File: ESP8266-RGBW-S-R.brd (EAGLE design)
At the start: 95.5 x 55.1 mm, 57 parts, among them IC1 ATTINY85, IC2 ESP8266-ESP12, IC6 LM1117-3.3, K1 SONGLE-RELAY-SPDT, K2 OMRON-G3MB-OPTO-RELAY, Q1 BC317, Q2 BC317, Q3 SO340020, Q4 SO340020, Q5 SO340020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

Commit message: added White channel for PWM output
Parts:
- removed JP4: (no value), Aidans:HDR4X0.1
- added J1: DCJ0202, con-jack:DCJ0202
- added Q6: SO340020, transistor-fet:SOT23
- added R20: 1K, resistor:R0805
- added X1: JST-XH-05-PIN-LONG-PAD, Rembrandt Electronics - JST XH Connectors v1-0:JST-XH-05-PACKAGE-LONG-PAD
- moved R19 8.98 mm to (52.5, 7.90)
- moved Q3 7.11 mm to (53.6, 14.5)
- moved Q4 7.11 mm to (58.3, 14.4)
- moved Q5 6.86 mm to (62.7, 14.4)
- moved R18 4.33 mm to (46.7, 9.75)
- moved R17 2.55 mm to (55.6, 8.92)
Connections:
- removed net N$152: IC2.TXD, JP10.5, WIFI2.1
- new net GPIO3: IC2.TXD, JP10.5, R20.2, WIFI2.1
- new net N$117: Q3.3, X1.5
- new net N$118: Q6.1, R20.1
- net GND: now also J1.3, Q6.2
- net N$12: now also Q6.3, X1.2; no longer JP4.4, Q3.3
- net N$14: now also Q5.3, X1.3; no longer JP4.3, Q4.3
- net N$79: now also Q4.3, X1.4; no longer JP4.2, Q5.3
- net N$80: now also X1.1; no longer JP4.1
- net VCC: now also J1.1
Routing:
- net GPIO3: track 0.00 -> 107.8 mm, vias 0 -> 1
- net N$152: track 33.8 -> 0.00 mm
- net N$117: track 0.00 -> 27.8 mm
- net GPIO4: track 87.4 -> 73.7 mm, vias 5 -> 4
- net N$3: track 16.6 -> 30.1 mm
- net N$81: track 13.3 -> 0.00 mm
- net GND: track 118.1 -> 107.0 mm, vias 6 -> 9
- net GPIO15: track 99.7 -> 94.6 mm
- net N$118: track 0.00 -> 4.47 mm
- net GPIO5: track 62.3 -> 58.1 mm
- net N$12: track 21.5 -> 17.6 mm
- net N$113: track 4.03 -> 7.29 mm
- net N$112: track 16.0 -> 18.5 mm
- net N$79: track 19.2 -> 21.4 mm
- net N$80: track 3.55 -> 4.67 mm
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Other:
- board text added: "W"

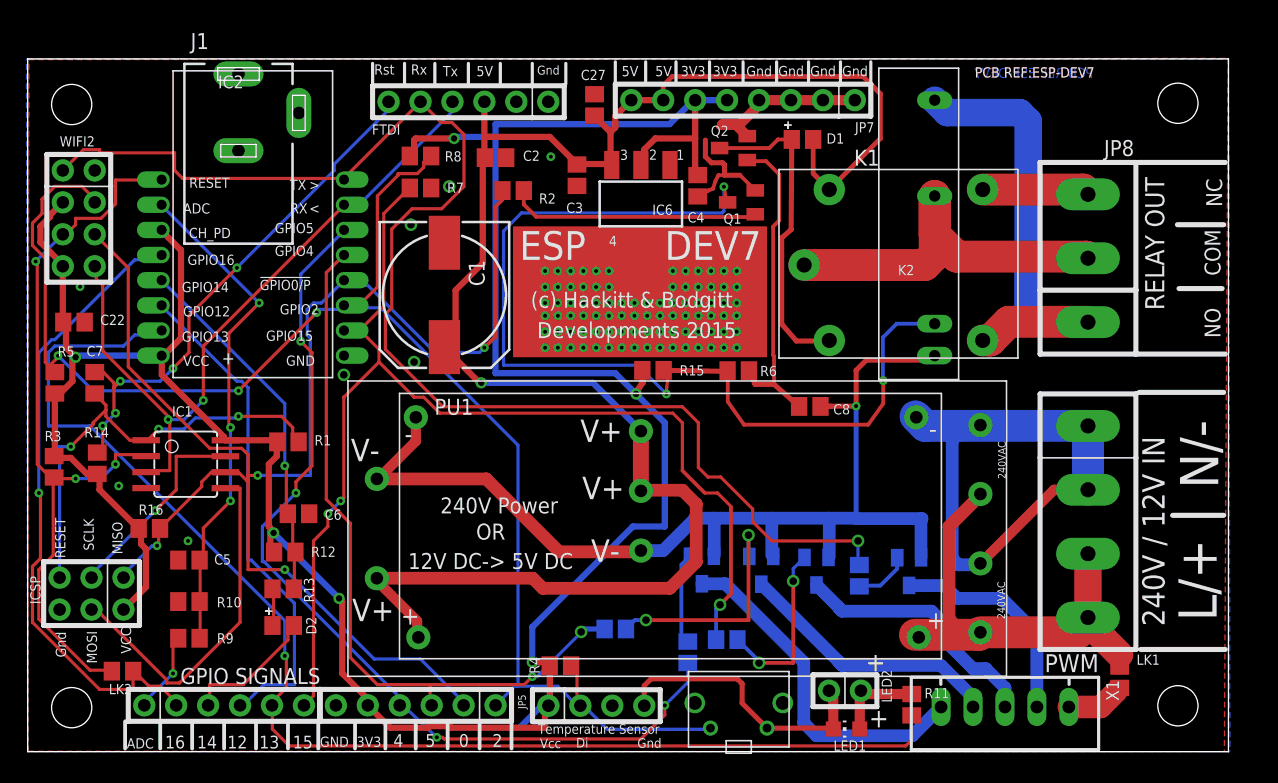
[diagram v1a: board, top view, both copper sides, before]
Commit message: alternative power subbly (DC-DC, AC-DC), alternative power jack as input
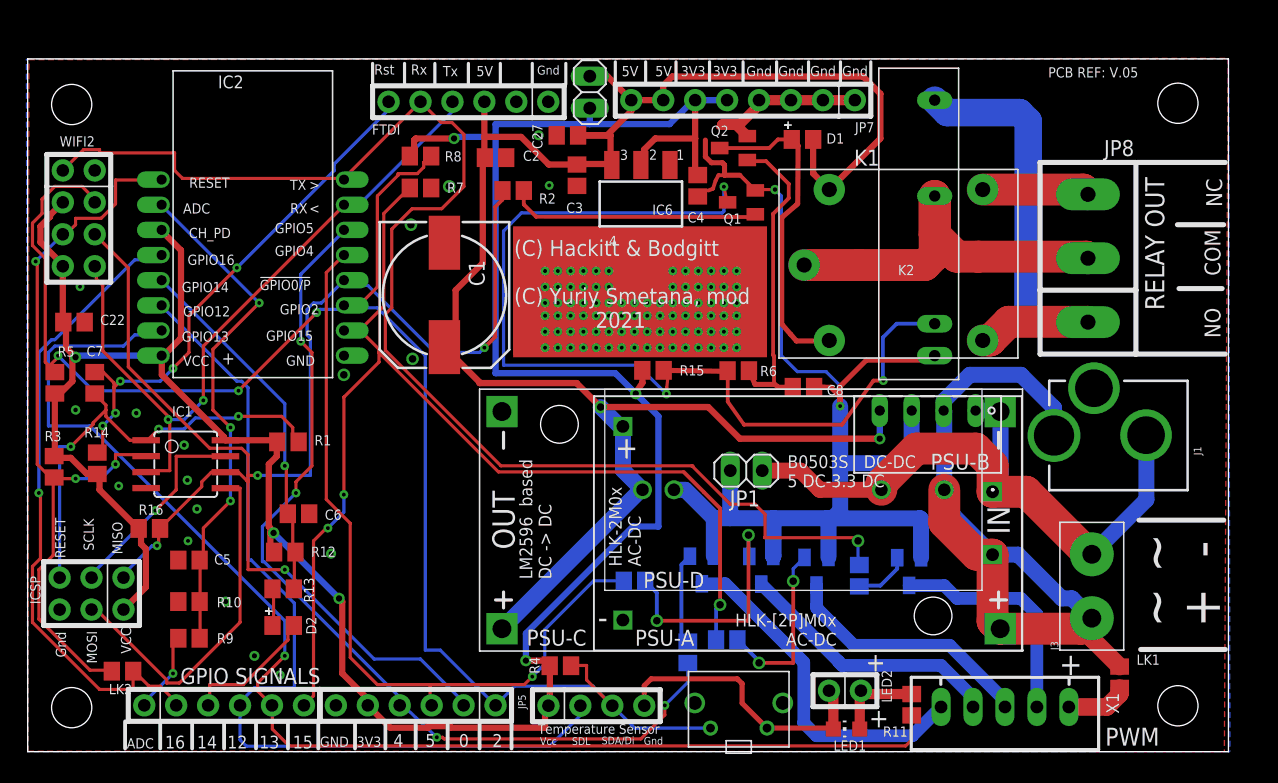
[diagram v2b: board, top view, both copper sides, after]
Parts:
- removed PU1: MAINS_PSU_CHEAP_CHINESE, Aidans:MAINS_PSU_CHEAP_CHINESE
- added J3: WJ300-5.0, SparkFun-Connectors-2pin:1X02_XTRA_BIG
- added JP4: V+V, pinhead:1X02
- added PSU-A: HLK-PM013W, 5:HLK-PM01
- added PSU-B: B0503S, dc-dc-converter:NME
- added PSU-C: DC-DC-STEP-DOWN-LM2596, diy-modules:DC-DC-STEP-DOWN-LM2596
- added PSU-D: HLK-2M03, HLK-2M03:HLK2M03
- J1: value DCJ0202 -> POWER_JACKPTH_LOCK; device con-jack:DCJ0202 -> SparkFun-Connectors:POWER_JACK_PTH_LOCK
- JP1: value 240V In -> GND+GND; device Aidans:4X0.2 -> pinhead:1X02
- moved J1 82.8 mm to (95.5, 25.1), turned to 90 degrees
- moved JP1 27.4 mm to (57.1, 22.4)
- moved R18 4.10 mm to (48.3, 13.6)
- moved C27 3.24 mm to (42.9, 49.0), turned to 180 degrees
- moved C8 1.61 mm to (61.7, 29.0)
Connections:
- removed net N$3: JP1.1, JP1.2, PU1.240V-A
- removed net N$5: JP1.3, JP1.4, LK1.1, PU1.240V-B
- new net +VCC: C1.+, C2.1, C27.1, C3.1, D1.C, IC6.3, JP10.3, JP4.1, JP7.7, JP7.8, K1.C1, PSU-A.P$4
- new net V+: J1.PWR, J3.1, LK1.1, PSU-A.P$1, PSU-B.2, PSU-C.IN+, PSU-D.1
- new net V-: J1.GND, J3.2, PSU-A.P$2, PSU-B.1, PSU-C.IN-, PSU-D.2
- net +3V3: now also JP4.2
- net GND: now also JP1.1, JP1.2, PSU-A.P$3, PSU-B.3, PSU-C.OUT-, PSU-D.3; no longer J1.3, PU1.V-
- net GPIO2: now also JP5.3; no longer JP5.2
- net N$11: now also JP5.2
- net VCC: now also PSU-B.4, PSU-C.OUT+, PSU-D.4; no longer C1.+, C2.1, C27.1, C3.1, D1.C, IC6.3, J1.1, JP10.3, JP7.7, JP7.8, K1.C1, PU1.V+
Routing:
- net +VCC: track 0.00 -> 125.1 mm, vias 0 -> 2
- net VCC: track 93.8 -> 21.5 mm, vias 1 -> 0
- net V-: track 0.00 -> 63.1 mm
- net V+: track 0.00 -> 62.8 mm
- net GND: track 107.0 -> 143.5 mm, vias 9 -> 20
- net N$11: track 39.9 -> 72.0 mm
- net N$3: track 30.1 -> 0.00 mm
- net N$5: track 18.9 -> 0.00 mm
- net N$114: track 5.11 -> 0.00 mm
- net GPIO5: track 58.1 -> 62.8 mm, vias 2 -> 1
- net GPIO2: track 125.7 -> 129.5 mm
- net GPIO15: track 94.6 -> 91.4 mm
- net +3V3: track 224.0 -> 222.2 mm
- net GPIO3: track 107.8 -> 106.4 mm
- net N$2: track 39.9 -> 40.9 mm
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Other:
- board text added: "(C) Hackitt & Bodgitt (C) Yuriy Smetana, mod 2021"
- board text added: "5V+3V3"
- board text added: "B0503S 5 DC-3.3 DC"
- board text added: "HLK-2M0x AC-DC"
- board text added: "HLK-[2P]M0x AC-DC"
- board text added: "LM2596 based DC -> DC"
- board text added: "PCB REF: V.05"
- board text added: "SDA/Di"
- board text added: "SDL"
- board text added: "~ ~ + -"
- board text removed: "(c) Hackitt & Bodgitt"
- board text removed: "12V DC-> 5V DC"
- board text removed: "240V / 12V IN"
- board text removed: "240V Power"
- board text removed: "DEV7"
- board text removed: "Developments 2015"
- board text removed: "Di"
- board text removed: "ESP"
- board text removed: "L/+"
- board text removed: "N/-"
- board text removed: "OR"
- board text removed: "PCB REF:ESP-DEV7"

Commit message: v 0.6
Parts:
- added R21: 4K7, resistor:R0805
- moved R5 50.7 mm to (47.4, 6.58), turned to 0 degrees
- moved R4 46.1 mm to (2.16, 29.3), turned to 270 degrees
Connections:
- net +3V3: now also R21.2, R4.2, R5.1; no longer R4.1, R5.2
- net GPIO2: now also R4.1, R5.2; no longer R4.2, R5.1
- net N$11: now also R21.1
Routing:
- net +3V3: track 222.2 -> 230.3 mm
- net N$11: track 72.0 -> 75.0 mm
- net GPIO2: track 129.5 -> 126.6 mm
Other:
- board text added: "+12"
- board text added: "B0503S 5DC-3.3DC"
- board text added: "PCB REF: V.06"
- board text added: "SDA Di"
- board text removed: "B0503S 5 DC-3.3 DC"
- board text removed: "PCB REF: V.05"
- board text removed: "SDA/Di"

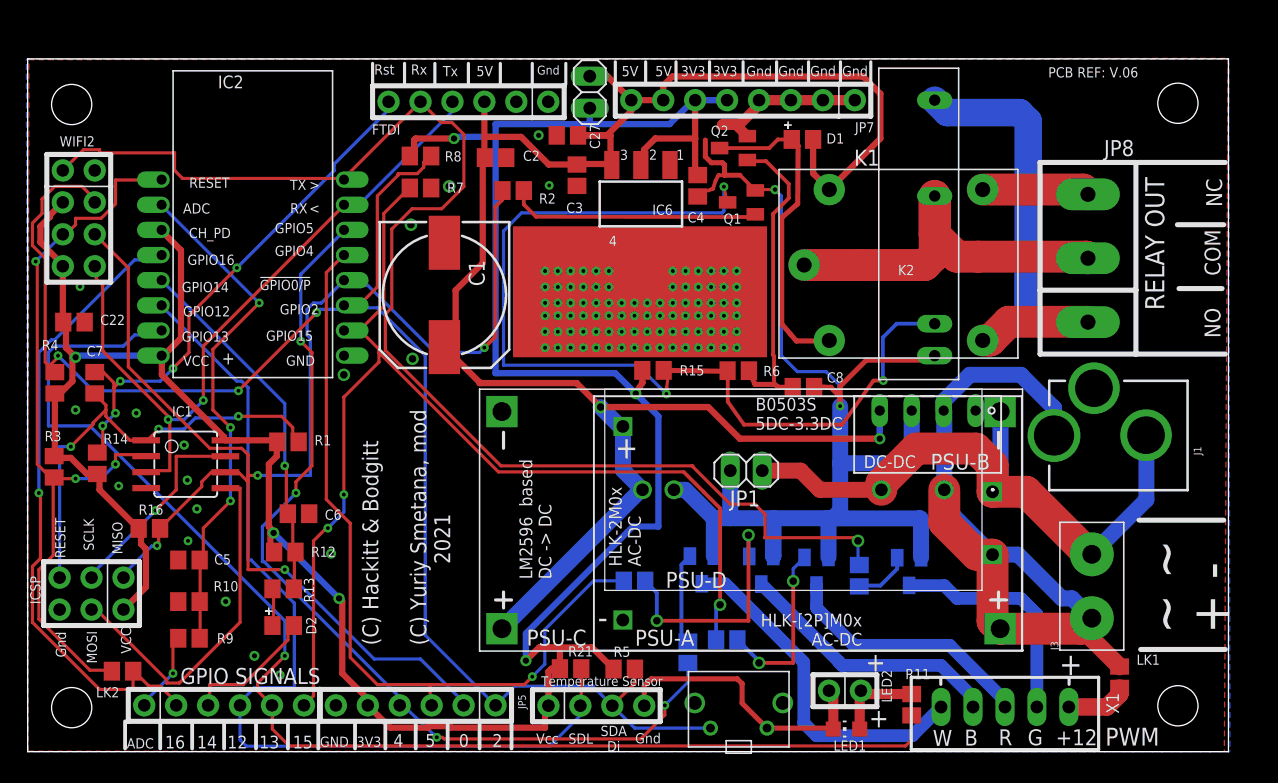
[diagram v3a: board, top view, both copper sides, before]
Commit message: pull down resistors for the PWM control, some silkprint correction
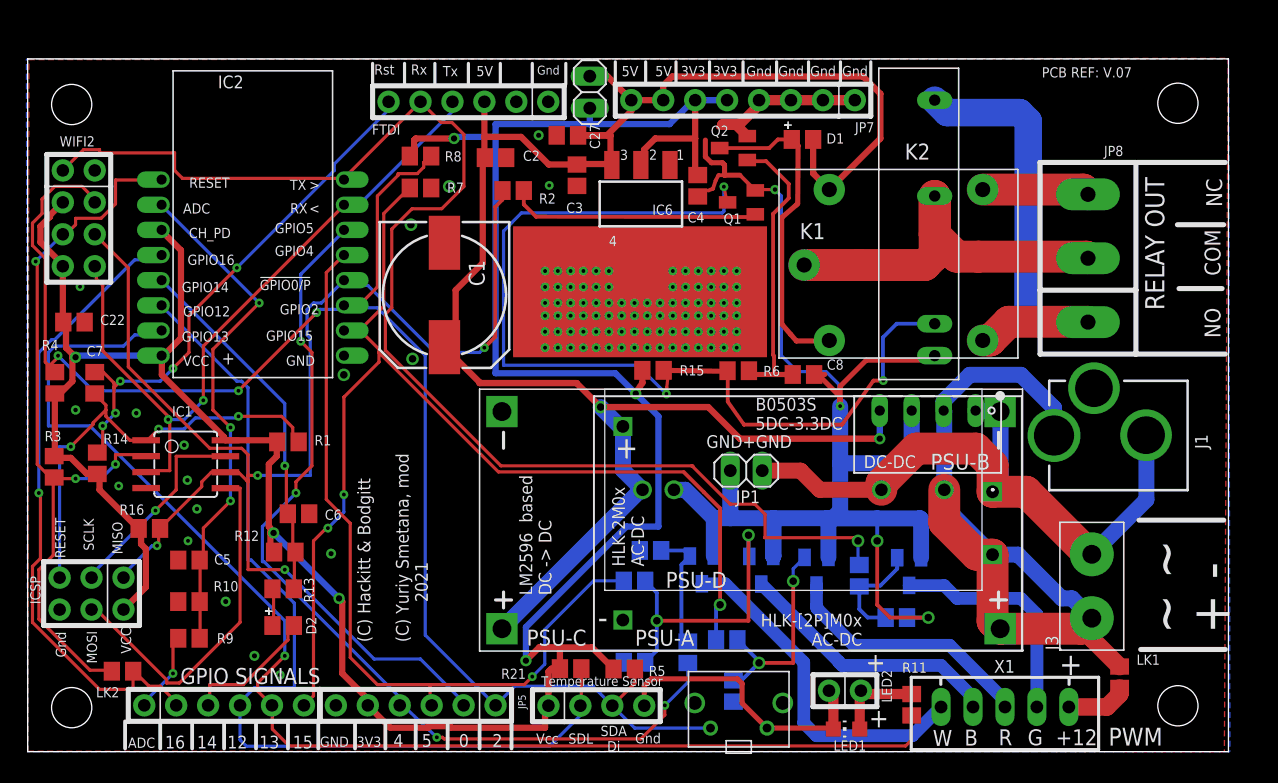
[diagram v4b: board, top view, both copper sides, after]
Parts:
- added R22, R23, R24, R25: 10K, resistor:R0805
- moved C8 1.02 mm to (61.7, 30.0)
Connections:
- net GND: now also R22.2, R23.2, R24.2, R25.2
- net N$112: now also R23.1
- net N$113: now also R24.1
- net N$118: now also R25.1
- net N$82: now also R22.1
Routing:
- net GND: track 143.5 -> 156.9 mm, vias 20 -> 22
- net N$118: track 4.47 -> 8.66 mm
- net N$112: track 19.4 -> 23.0 mm
- net N$82: track 14.0 -> 16.7 mm
- net N$113: track 7.29 -> 9.77 mm
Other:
- board text added: "GND+GND"
- board text added: "JLCJLCJLCJLC"
- board text added: "PCB REF: V.07"
- board text removed: "PCB REF: V.06"

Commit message: r11 moved
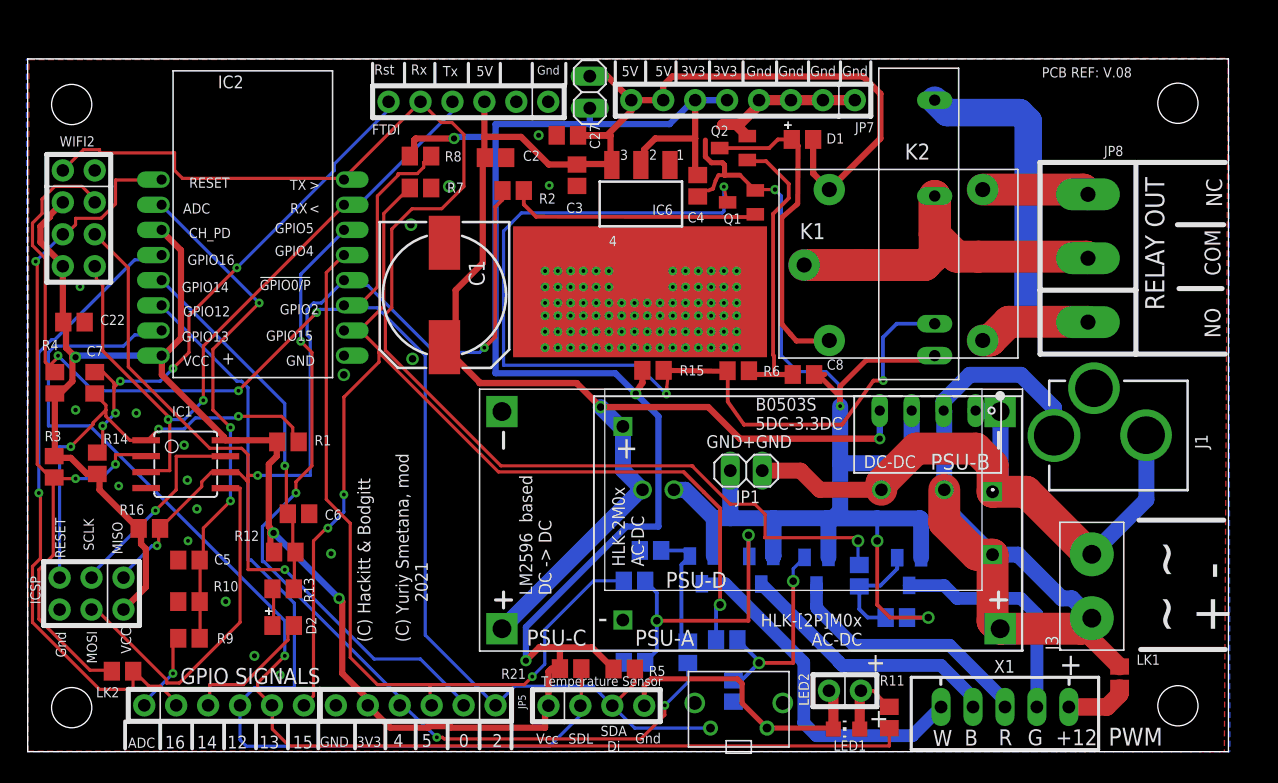
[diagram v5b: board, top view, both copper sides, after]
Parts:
- moved R11 2.05 mm to (68.5, 2.72)
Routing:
- net GPIO13: track 104.3 -> 101.8 mm
- net N$4: track 7.24 -> 5.88 mm
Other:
- board text added: "PCB REF: V.08"
- board text removed: "PCB REF: V.07"
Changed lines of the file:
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@@
 <layer number="20" name="Dimension" color="15" fill="1" visible="yes" active="yes"/>
 <layer number="21" name="tPlace" color="7" fill="1" visible="yes" active="yes"/>
-<layer number="22" name="bPlace" color="7" fill="1" visible="yes" active="yes"/>
+<layer number="22" name="bPlace" color="7" fill="1" visible="no" active="yes"/>
 <layer number="23" name="tOrigins" color="15" fill="1" visible="yes" active="yes"/>
-<layer number="24" name="bOrigins" color="15" fill="1" visible="yes" active="yes"/>
+<layer number="24" name="bOrigins" color="15" fill="1" visible="no" active="yes"/>
 <layer number="25" name="tNames" color="7" fill="1" visible="yes" active="yes"/>
-<layer number="26" name="bNames" color="7" fill="1" visible="yes" active="yes"/>
+<layer number="26" name="bNames" color="7" fill="1" visible="no" active="yes"/>
 <layer number="27" name="tValues" color="7" fill="1" visible="yes" active="yes"/>
-<layer number="28" name="bValues" color="7" fill="1" visible="yes" active="yes"/>
+<layer number="28" name="bValues" color="7" fill="1" visible="no" active="yes"/>
 <layer number="29" name="tStop" color="7" fill="3" visible="yes" active="yes"/>
-<layer number="30" name="bStop" color="7" fill="6" visible="yes" active="yes"/>
+<layer number="30" name="bStop" color="7" fill="6" visible="no" active="yes"/>
 <layer number="31" name="tCream" color="7" fill="4" visible="yes" active="yes"/>
-<layer number="32" name="bCream" color="7" fill="5" visible="yes" active="yes"/>
+<layer number="32" name="bCream" color="7" fill="5" visible="no" active="yes"/>
 <layer number="33" name="tFinish" color="6" fill="3" visible="yes" active="yes"/>
 <layer number="34" name="bFinish" color="6" fill="6" visible="yes" active="yes"/>
 <layer number="35" name="tGlue" color="7" fill="4" visible="yes" active="yes"/>
-<layer number="36" name="bGlue" color="7" fill="5" visible="yes" active="yes"/>
+<layer number="36" name="bGlue" color="7" fill="5" visible="no" active="yes"/>
 <layer number="37" name="tTest" color="7" fill="1" visible="yes" active="yes"/>
 <layer number="38" name="bTest" color="7" fill="1" visible="yes" active="yes"/>
@@
 <text x="4.445" y="18.542" size="0.8128" layer="21" rot="R270">SCLK</text>
 <text x="7.4168" y="9.8806" size="0.8128" layer="21" rot="R270">VCC</text>
-<text x="80.656" y="53.621" size="0.8128" layer="21">PCB REF: V.07</text>
+<text x="80.656" y="53.621" size="0.8128" layer="21">PCB REF: V.08</text>
 <wire x1="0" y1="0" x2="95.5" y2="0" width="0" layer="20"/>
 <wire x1="95.5" y1="0" x2="95.5" y2="55.1" width="0" layer="20"/>
@@
 <attribute name="VALUE" x="30.262" y="39.397" size="0.8128" layer="27" rot="R270"/>
 </element>
-<element name="R11" library="resistor" package="R0805" value="2k2" x="70.3072" y="3.7338" smashed="yes" rot="R270">
-<attribute name="NAME" x="69.5452" y="6.2738" size="0.8128" layer="25"/>
-<attribute name="VALUE" x="71.7296" y="3.2004" size="0.8128" layer="27"/>
+<element name="R11" library="resistor" package="R0805" value="2k2" x="68.5292" y="2.7178" smashed="yes" rot="R270">
+<attribute name="NAME" x="67.7672" y="5.2578" size="0.8128" layer="25"/>
+<attribute name="VALUE" x="67.6656" y="0.1524" size="0.8128" layer="27"/>
 </element>
 <element name="LED1" library="led" package="CHIP-LED0805" value="Indicator" x="65.1256" y="1.8034" smashed="yes" rot="R90">
@@
 </element>
 <element name="LED2" library="Aidans" package="HDR2X0.1" value="LED" x="66.2686" y="4.8514" smashed="yes" rot="R90">
-<attribute name="NAME" x="67.9196" y="6.5024" size="0.8128" layer="25" rot="R270"/>
+<attribute name="NAME" x="61.3156" y="6.2484" size="0.8128" layer="25" rot="R270"/>
 <attribute name="VALUE" x="66.1416" y="7.2644" size="0.8128" layer="27" rot="R180"/>
 </element>
@@
 <wire x1="66.2686" y1="4.8514" x2="66.1756" y2="4.7584" width="0.8128" layer="1"/>
 <wire x1="66.1756" y1="4.7584" x2="66.1756" y2="1.8034" width="0.8128" layer="1"/>
-<wire x1="66.2686" y1="4.8514" x2="66.5362" y2="4.5838" width="0.8128" layer="1"/>
-<wire x1="66.5362" y1="4.5838" x2="70.3072" y2="4.5838" width="0.8128" layer="1"/>
+<wire x1="66.2686" y1="4.8514" x2="66.2822" y2="4.8378" width="0.8128" layer="1"/>
+<wire x1="67.2592" y1="4.8378" x2="68.5292" y2="3.5678" width="0.254" layer="1"/>
+<wire x1="67.2592" y1="4.8378" x2="66.2822" y2="4.8378" width="0.254" layer="1"/>
 </signal>
 <signal name="N$8">
@@
 <contactref element="JP2" pad="5"/>
 <contactref element="R11" pad="2"/>
-<wire x1="70.3072" y1="2.8838" x2="70.2818" y2="2.8584" width="0.4064" layer="1"/>
-<wire x1="70.2818" y1="2.8584" x2="70.2818" y2="0.9144" width="0.254" layer="1"/>
-<wire x1="70.2818" y1="0.9144" x2="69.8246" y2="0.4572" width="0.254" layer="1"/>
+<wire x1="68.5292" y1="1.8678" x2="68.5292" y2="0.4572" width="0.254" layer="1"/>
 <wire x1="10.287" y1="33.147" x2="10.541" y2="33.401" width="0.254" layer="16"/>
 <wire x1="8.509" y1="33.147" x2="10.287" y2="33.147" width="0.254" layer="16"/>
@@
 <wire x1="10.541" y1="33.401" x2="10.653" y2="33.497" width="0.254" layer="16"/>
 <via x="20.447" y="7.62" extent="1-16" drill="0.3048"/>
-<wire x1="69.8246" y1="0.4572" x2="20.8026" y2="0.4572" width="0.254" layer="1"/>
+<wire x1="68.5292" y1="0.4572" x2="20.8026" y2="0.4572" width="0.254" layer="1"/>
 <wire x1="20.8026" y1="0.4572" x2="19.4564" y2="1.8034" width="0.254" layer="1"/>
 <wire x1="19.4564" y1="1.8034" x2="19.4564" y2="3.6576" width="0.254" layer="1"/>
